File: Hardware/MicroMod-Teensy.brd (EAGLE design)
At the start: 22 x 22.8 mm, 72 parts, among them J1 MICROMOD-2222, U1 IMXRT1062DV10X10, U2 W25QXX3X2, U3 MKL02Z32VFG4, Y1 32.768kHz, Y2 24MHz

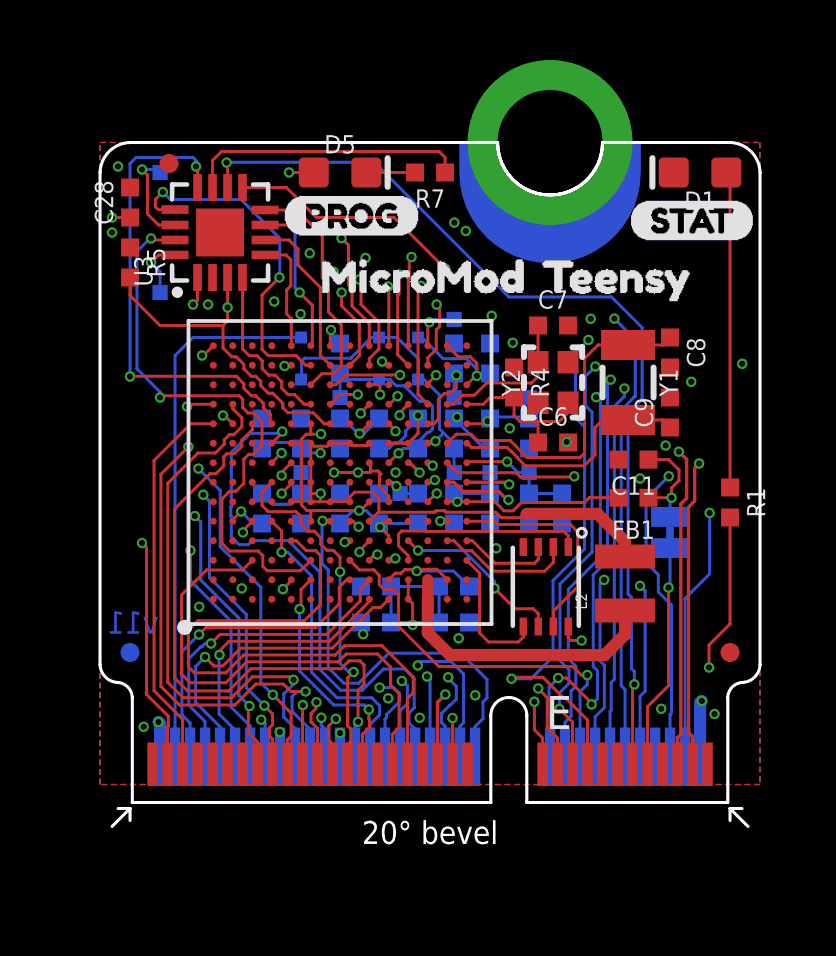
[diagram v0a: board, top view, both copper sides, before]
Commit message: Add power control circuitry.
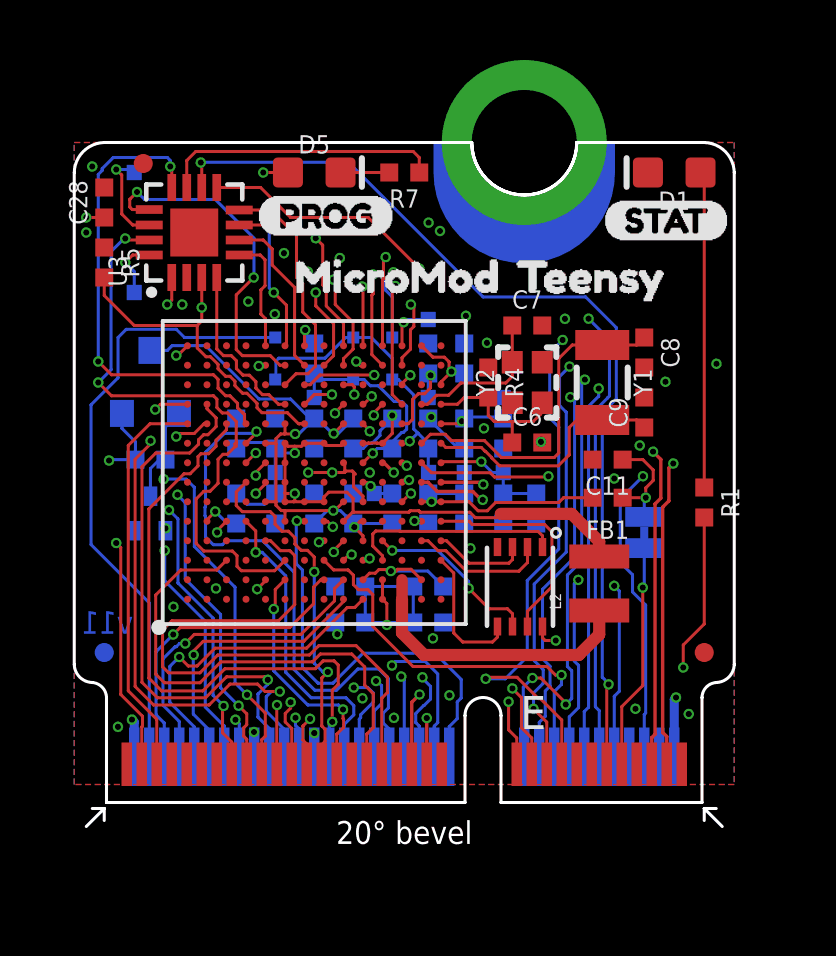
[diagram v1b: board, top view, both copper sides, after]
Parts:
- added Q1: 20V/4.2A/52mΩ/1.4W, SparkFun-DiscreteSemi:SOT23-3
- added Q2: 20V/0.2A/8MHz/1.2Ω/1Vth, SparkFun-DiscreteSemi:SOT-416FL
- added R2: 100k, SparkFun-Resistors:0402-TIGHT
- moved U$5 0.86 mm to (20.7, 15.5)
- moved U$6 0.86 mm to (16.7, 19.4)
- moved U$7 0.86 mm to (20.2, 6.60)
- moved Y1 0.86 mm to (16.7, 14.0)
- moved C1 0.86 mm to (8.44, 12.3)
- moved C10 0.86 mm to (10.9, 7.20)
- moved C13 0.86 mm to (10.9, 9.80)
- moved C14 0.86 mm to (10.9, 6.00)
- moved C22 0.86 mm to (10.9, 12.3)
- moved C23 0.86 mm to (10.9, 14.8)
- moved C25 0.86 mm to (13.4, 9.80)
- moved C26 0.86 mm to (13.4, 12.3)
- moved C27 0.86 mm to (14.5, 9.80)
- moved C5 0.86 mm to (8.44, 9.80)
- moved D4 0.86 mm to (8.44, 14.8)
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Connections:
- new net 3.3V_CONTROLLED: C1.1, C2.1, C3.1, C4.1, C5.1, Q1.3, R6.1, U1.E6, U1.E9, U1.F10, U1.F5, U1.J10, U1.J6, U1.K4, U1.K5, U1.N14, U1.P12
- new net N$7: Q1.1, Q2.3, R2.2
- net 3.3V: now also Q1.2, R2.1; no longer C1.1, C2.1, C3.1, C4.1, C5.1, R6.1, U1.E6, U1.E9, U1.F10, U1.F5, U1.J10, U1.J6, U1.K4, U1.K5, U1.N14, U1.P12
- net GND: now also Q2.2
- net PMIC: now also Q2.1; no longer J1.4
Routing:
- net 3.3V_CONTROLLED: track 0.00 -> 28.5 mm, vias 0 -> 5
- net 3.3V: track 24.9 -> 12.1 mm, vias 12 -> 9
- net PMIC: track 20.5 -> 8.78 mm
- net N$7: track 0.00 -> 3.27 mm
- net V_BATT: track 17.8 -> 20.6 mm
- net GND: track 26.7 -> 27.5 mm
- net DEBUG_EN: track 19.3 -> 20.0 mm
- net SCK/13: track 35.8 -> 36.5 mm

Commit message: Adding panel files
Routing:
- net GPIO/32: track 20.0 -> 20.8 mm

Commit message: Remove cream from test points
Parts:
- TP10, TP11, TP2, TP3, TP4, TP5, TP6, TP7, TP8, TP9: value (none) -> TEST-POINT2
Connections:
- net N$1: now also TP1.1; no longer TP1.P$1
- net N$30: now also TP5.1; no longer TP5.P$1
- net N$33: now also TP6.1; no longer TP6.P$1
- net N$34: now also TP7.1; no longer TP7.P$1
- net PMIC: now also TP2.1; no longer TP2.P$1
- net SWD_CLK: now also TP9.1; no longer TP9.P$1
- net SWD_DIO: now also TP8.1; no longer TP8.P$1
- net VCC: now also TP3.1; no longer TP3.P$1
- net VDD_SNVS_IN: now also TP4.1; no longer TP4.P$1
- net VDD_SOC_IN: now also TP10.1; no longer TP10.P$1
- net VDD_USB_CAP: now also TP11.1; no longer TP11.P$1
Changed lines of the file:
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@@
 <attribute name="VALUE" x="11.502" y="9.8" size="0.6096" layer="28" font="vector" ratio="20" rot="MR270" align="top-center"/>
 </element>
-<element name="TP3" library="SparkFun-Connectors" package="PAD.02X.02" value="" x="12.14" y="11" smashed="yes" rot="MR90"/>
+<element name="TP3" library="SparkFun-Connectors" package="PAD.02X.02" value="TEST-POINT2" x="12.14" y="11" smashed="yes" rot="MR90"/>
 <element name="C14" library="SparkFun-Capacitors" package="0402-TIGHT" value="4.7uF" x="10.94" y="6" smashed="yes" rot="MR180">
 <attribute name="NAME" x="10.94" y="5.438" size="0.6096" layer="26" font="vector" ratio="20" rot="MR180" align="bottom-center"/>
@@
 <attribute name="VALUE" x="10.378" y="12.3" size="0.6096" layer="28" font="vector" ratio="20" rot="MR90" align="top-center"/>
 </element>
-<element name="TP4" library="SparkFun-Connectors" package="PAD.02X.02" value="" x="10.95" y="11" smashed="yes" rot="MR0"/>
+<element name="TP4" library="SparkFun-Connectors" package="PAD.02X.02" value="TEST-POINT2" x="10.95" y="11" smashed="yes" rot="MR0"/>
 <element name="C23" library="SparkFun-Capacitors" package="0402-TIGHT" value="0.22uF" x="10.94" y="14.8" smashed="yes" rot="MR90">
 <attribute name="NAME" x="11.502" y="14.8" size="0.6096" layer="26" font="vector" ratio="20" rot="MR90" align="bottom-center"/>
@@
 <attribute name="VALUE" x="15.102" y="9.8" size="0.6096" layer="28" font="vector" ratio="20" rot="MR270" align="top-center"/>
 </element>
-<element name="TP5" library="SparkFun-Connectors" package="PAD.02X.02" value="" x="10.94" y="13.5" smashed="yes" rot="MR0"/>
-<element name="TP6" library="SparkFun-Connectors" package="PAD.02X.02" value="" x="13.44" y="13.5" smashed="yes" rot="MR0"/>
-<element name="TP7" library="SparkFun-Connectors" package="PAD.02X.02" value="" x="13.44" y="11" smashed="yes" rot="MR0"/>
+<element name="TP5" library="SparkFun-Connectors" package="PAD.02X.02" value="TEST-POINT2" x="10.94" y="13.5" smashed="yes" rot="MR0"/>
+<element name="TP6" library="SparkFun-Connectors" package="PAD.02X.02" value="TEST-POINT2" x="13.44" y="13.5" smashed="yes" rot="MR0"/>
+<element name="TP7" library="SparkFun-Connectors" package="PAD.02X.02" value="TEST-POINT2" x="13.44" y="11" smashed="yes" rot="MR0"/>
 <element name="FD1" library="SparkFun-Aesthetics" package="FIDUCIAL-MICRO" value="FIDUCIALUFIDUCIAL" x="20.14" y="5" smashed="yes"/>
 <element name="FD2" library="SparkFun-Aesthetics" package="FIDUCIAL-MICRO" value="FIDUCIALUFIDUCIAL" x="1.44" y="21.3" smashed="yes"/>
@@
 <attribute name="VALUE" x="7.14" y="20.365" size="0.6096" layer="27" font="vector" ratio="20" align="top-center"/>
 </element>
-<element name="TP8" library="SparkFun-Connectors" package="PAD.02X.02" value="" x="1.14" y="17" smashed="yes" rot="MR0"/>
-<element name="TP9" library="SparkFun-Connectors" package="PAD.02X.02" value="" x="1.14" y="21" smashed="yes" rot="MR0"/>
+<element name="TP8" library="SparkFun-Connectors" package="PAD.02X.02" value="TEST-POINT2" x="1.14" y="17" smashed="yes" rot="MR0"/>
+<element name="TP9" library="SparkFun-Connectors" package="PAD.02X.02" value="TEST-POINT2" x="1.14" y="21" smashed="yes" rot="MR0"/>
 <element name="C28" library="SparkFun-Capacitors" package="0402-TIGHT" value="0.22uF" x="0.14" y="20" smashed="yes" rot="R90">
 <attribute name="NAME" x="-0.422" y="20" size="0.6096" layer="25" font="vector" ratio="20" rot="R90" align="bottom-center"/>
@@
 <attribute name="VALUE" x="0.702" y="20" size="0.6096" layer="27" font="vector" ratio="20" rot="R90" align="top-center"/>
 </element>
-<element name="TP10" library="SparkFun-Connectors" package="PAD.02X.02" value="" x="5.84" y="11" smashed="yes" rot="MR270"/>
-<element name="TP11" library="SparkFun-Connectors" package="PAD.02X.02" value="" x="7.14" y="13.5" smashed="yes" rot="MR270"/>
+<element name="TP10" library="SparkFun-Connectors" package="PAD.02X.02" value="TEST-POINT2" x="5.84" y="11" smashed="yes" rot="MR270"/>
+<element name="TP11" library="SparkFun-Connectors" package="PAD.02X.02" value="TEST-POINT2" x="7.14" y="13.5" smashed="yes" rot="MR270"/>
 <element name="U$2" library="buzzard_labels (1)" package="MICROMOD0" value="" x="5.586" y="17.526" smashed="yes"/>
 <element name="U$3" library="buzzard_labels (1)" package="TEENSY2" value="" x="12.998" y="17.526" smashed="yes"/>
@@
 <element name="U$7" library="SparkFun-Buzzard" package="MEAS_32" value="" x="20.24" y="6.6" smashed="yes" rot="MR90"/>
 <element name="J1" library="Teensy" package="M.2-CARD-E-22" value="MICROMOD-2222" x="10.14" y="0" smashed="yes"/>
-<element name="TP2" library="SparkFun-Connectors" package="PAD.02X.02" value="" x="9.14" y="10.3" smashed="yes" rot="MR0"/>
+<element name="TP2" library="SparkFun-Connectors" package="PAD.02X.02" value="TEST-POINT2" x="9.14" y="10.3" smashed="yes" rot="MR0"/>
 <element name="Q1" library="SparkFun-DiscreteSemi" package="SOT23-3" value="20V/4.2A/52mΩ/1.4W" x="1.68" y="13.97" smashed="yes" rot="MR0">
 <attribute name="NAME" x="3.331" y="13.97" size="0.6096" layer="26" font="vector" ratio="20" rot="MR90" align="bottom-center"/>
@@
 <signal name="N$1">
 <contactref element="U1" pad="M14"/>
-<contactref element="TP1" pad="P$1"/>
+<contactref element="TP1" pad="1"/>
 <wire x1="10.94" y1="16.1" x2="10.20955" y2="16.1" width="0.1016" layer="16"/>
 <wire x1="10.20955" y1="16.1" x2="10.11955" y2="16.01" width="0.1016" layer="16"/>
@@
 <signal name="PMIC">
 <contactref element="U1" pad="K7"/>
-<contactref element="TP2" pad="P$1"/>
+<contactref element="TP2" pad="1"/>
 <wire x1="8.765" y1="10.655" x2="8.765" y2="10.675" width="0.1016" layer="1"/>
 <wire x1="9.14" y1="10.3" x2="9.0178" y2="10.4222" width="0.1016" layer="16"/>
@@
 <contactref element="C13" pad="1"/>
 <contactref element="C12" pad="1"/>
-<contactref element="TP3" pad="P$1"/>
+<contactref element="TP3" pad="1"/>
 <via x="11.05" y="10.025" extent="1-16" drill="0.2"/>
 <wire x1="10.94" y1="10.3" x2="12.14" y2="10.3" width="0.1016" layer="16"/>
@@
 <contactref element="U1" pad="F8"/>
 <contactref element="U1" pad="H6"/>
-<contactref element="TP10" pad="P$1"/>
+<contactref element="TP10" pad="1"/>
 <wire x1="4.54" y1="11.8" x2="4.74" y2="12" width="0.1016" layer="16"/>
 <wire x1="5.64" y1="12" x2="4.74" y2="12" width="0.1016" layer="16"/>
@@
 <contactref element="C21" pad="1"/>
 <contactref element="D4" pad="A"/>
-<contactref element="TP11" pad="P$1"/>
+<contactref element="TP11" pad="1"/>
 <wire x1="7.14" y1="14.3" x2="7.14" y2="13.5" width="0.1016" layer="16"/>
 <wire x1="8.765" y1="11.325" x2="9.079815625" y2="11.639815625" width="0.1016" layer="1"/>
@@
 <contactref element="U1" pad="M9"/>
 <contactref element="C22" pad="1"/>
-<contactref element="TP4" pad="P$1"/>
+<contactref element="TP4" pad="1"/>
 <contactref element="D4" pad="C"/>
 <contactref element="D2" pad="C"/>
@@
 <contactref element="U1" pad="M10"/>
 <contactref element="C23" pad="1"/>
-<contactref element="TP5" pad="P$1"/>
+<contactref element="TP5" pad="1"/>
 <via x="11.020184375" y="14.239815625" extent="1-16" drill="0.2"/>
 <wire x1="10.26905" y1="12.625" x2="10.41465" y2="12.7706" width="0.1016" layer="1"/>
@@
 <contactref element="C24" pad="1"/>
 <contactref element="C26" pad="1"/>
-<contactref element="TP6" pad="P$1"/>
+<contactref element="TP6" pad="1"/>
 <wire x1="11.365" y1="12.625" x2="11.975" y2="12.625" width="0.1016" layer="1"/>
 <wire x1="11.975" y1="12.625" x2="12.06" y2="12.71" width="0.1016" layer="1"/>
@@
 <contactref element="C25" pad="1"/>
 <contactref element="C27" pad="1"/>
-<contactref element="TP7" pad="P$1"/>
+<contactref element="TP7" pad="1"/>
 <wire x1="13.44" y1="11" x2="13.44" y2="10.3" width="0.1016" layer="16"/>
 <wire x1="14.54" y1="10.3" x2="13.44" y2="10.3" width="0.1016" layer="16"/>
@@
 <signal name="SWD_CLK">
 <contactref element="U3" pad="14"/>
-<contactref element="TP9" pad="P$1"/>
+<contactref element="TP9" pad="1"/>
 <wire x1="1.64" y1="19.25" x2="1.09" y2="19.25" width="0.1016" layer="1"/>
 <via x="0.54" y="21.1" extent="1-16" drill="0.2"/>
@@
 <signal name="SWD_DIO">
 <contactref element="U3" pad="16"/>
-<contactref element="TP8" pad="P$1"/>
+<contactref element="TP8" pad="1"/>
 <wire x1="1.64" y1="18.25" x2="1.09" y2="18.25" width="0.1016" layer="1"/>
 <wire x1="1.09" y1="18.25" x2="0.84" y2="18" width="0.1016" layer="1"/>

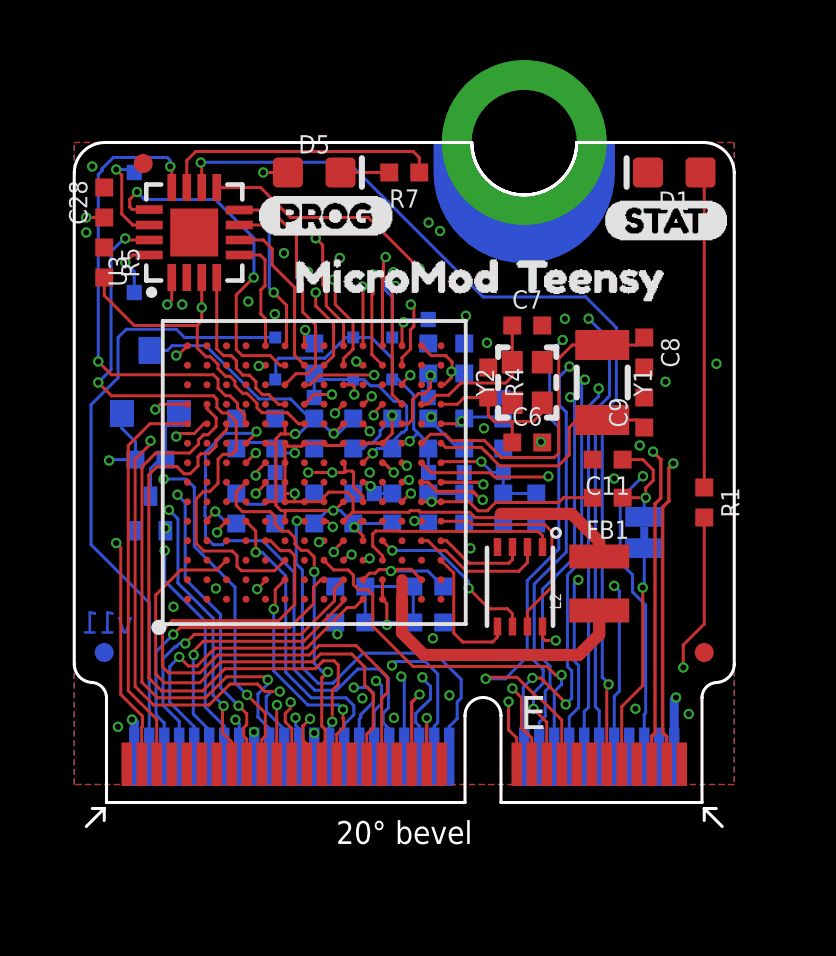
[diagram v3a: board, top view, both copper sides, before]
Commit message: Matches trace lenths to flash. New panel.
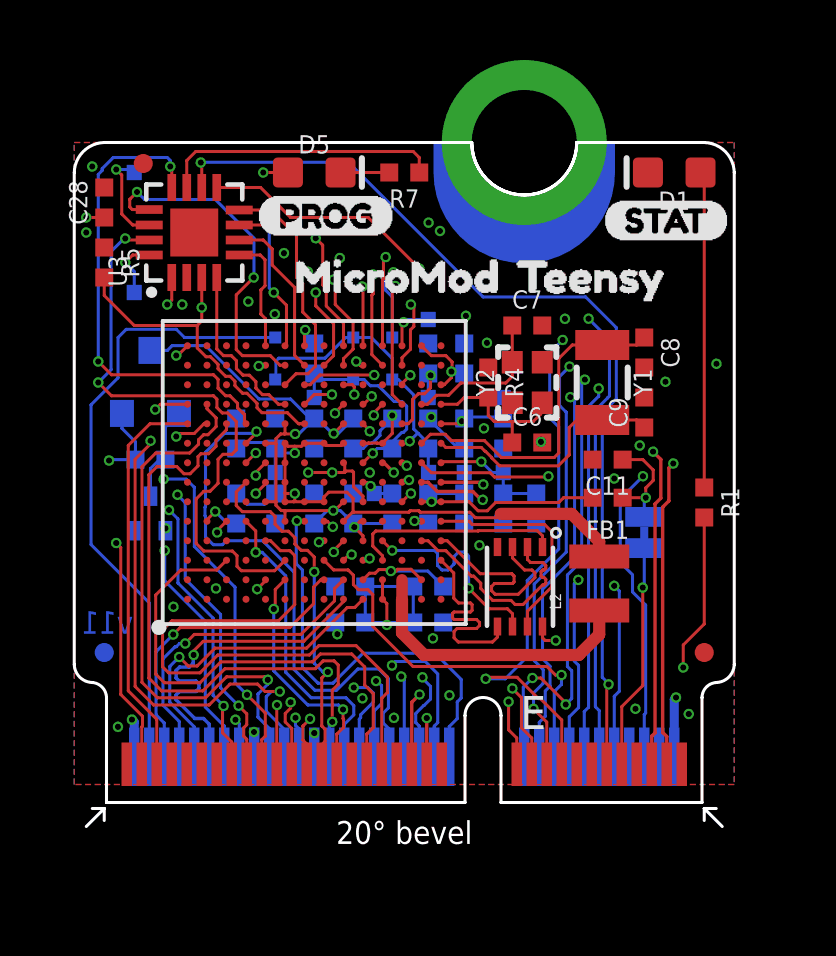
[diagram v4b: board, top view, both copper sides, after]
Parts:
- TP1: value 32kHz Test -> (none)
- TP10, TP11, TP2, TP3, TP4, TP5, TP6, TP7, TP8, TP9: value TEST-POINT2 -> (none)
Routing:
- net QSPI2: track 3.16 -> 7.39 mm
- net QSPI1: track 4.59 -> 7.32 mm
- net QSPI0: track 4.60 -> 7.31 mm
- net 35/DAT0: track 9.51 -> 11.6 mm
- net USB_D-: track 20.4 -> 22.2 mm
- net QSPI-CLK: track 6.02 -> 7.39 mm

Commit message: Route bus pins to v11.
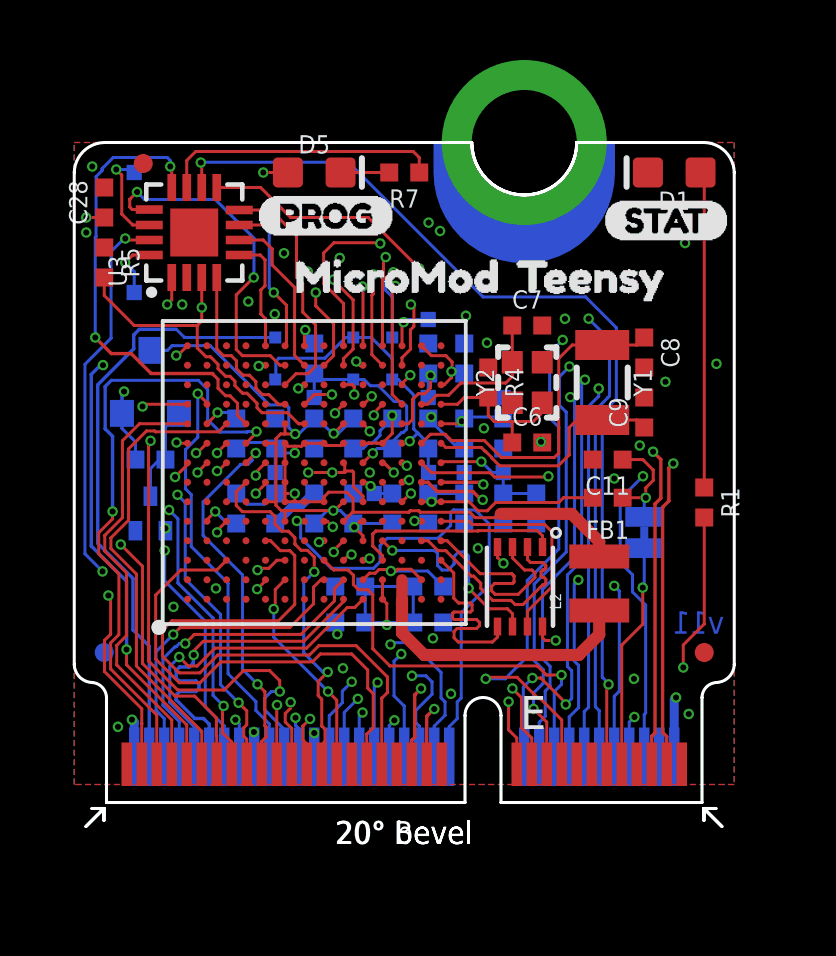
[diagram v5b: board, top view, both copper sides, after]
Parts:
- added LOGO2: OSHW-LOGONO_SILK, SparkFun-Aesthetics:DUMMY
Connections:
- new net GPIO/40: J1.40, U1.C8
- new net GPIO/41: J1.42, U1.B8
- new net GPIO/42: J1.44, U1.A8
- new net GPIO/43: J1.46, U1.A9
- new net GPIO/44: J1.48, U1.B9
- new net GPIO/45: J1.73, U1.C9
- net GPIO/26/A12: now also J1.67; no longer J1.42
- net GPIO/27/A13: now also J1.8; no longer J1.44
- net GPIO/28: no longer J1.46
- net GPIO/32: now also J1.65; no longer J1.48
- net GPIO/33: now also J1.63; no longer J1.73
- net GPIO/6: now also J1.71; no longer J1.40
- net GPIO/9: now also J1.69; no longer J1.71
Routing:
- net GPIO/44: track 0.00 -> 29.3 mm, vias 0 -> 2
- net GPIO/43: track 0.00 -> 26.1 mm, vias 0 -> 2
- net GPIO/42: track 0.00 -> 23.7 mm, vias 0 -> 2
- net GPIO/41: track 0.00 -> 22.1 mm, vias 0 -> 2
- net GPIO/40: track 0.00 -> 18.7 mm, vias 0 -> 2
- net GPIO/45: track 0.00 -> 15.3 mm, vias 0 -> 2
- net GPIO/28: track 10.3 -> 0.00 mm, vias 1 -> 0
- net GPIO/27/A13: track 24.9 -> 33.5 mm, vias 2 -> 3
- net GPIO/32: track 20.8 -> 15.6 mm, vias 1 -> 0
- net AUD_OUT/7: track 18.8 -> 13.9 mm
- net GPIO/26/A12: track 17.8 -> 21.9 mm, vias 2 -> 3
- net A0/14: track 23.8 -> 20.1 mm
- net PWM0/3: track 14.3 -> 17.5 mm
- net GND: track 27.4 -> 30.4 mm
- net GPIO/6: track 18.8 -> 20.9 mm, vias 1 -> 2
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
